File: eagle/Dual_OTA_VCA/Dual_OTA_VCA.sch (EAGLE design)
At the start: 31 parts, among them IC1 LM13600N, IC2 NJM4580, T1 2SA1015

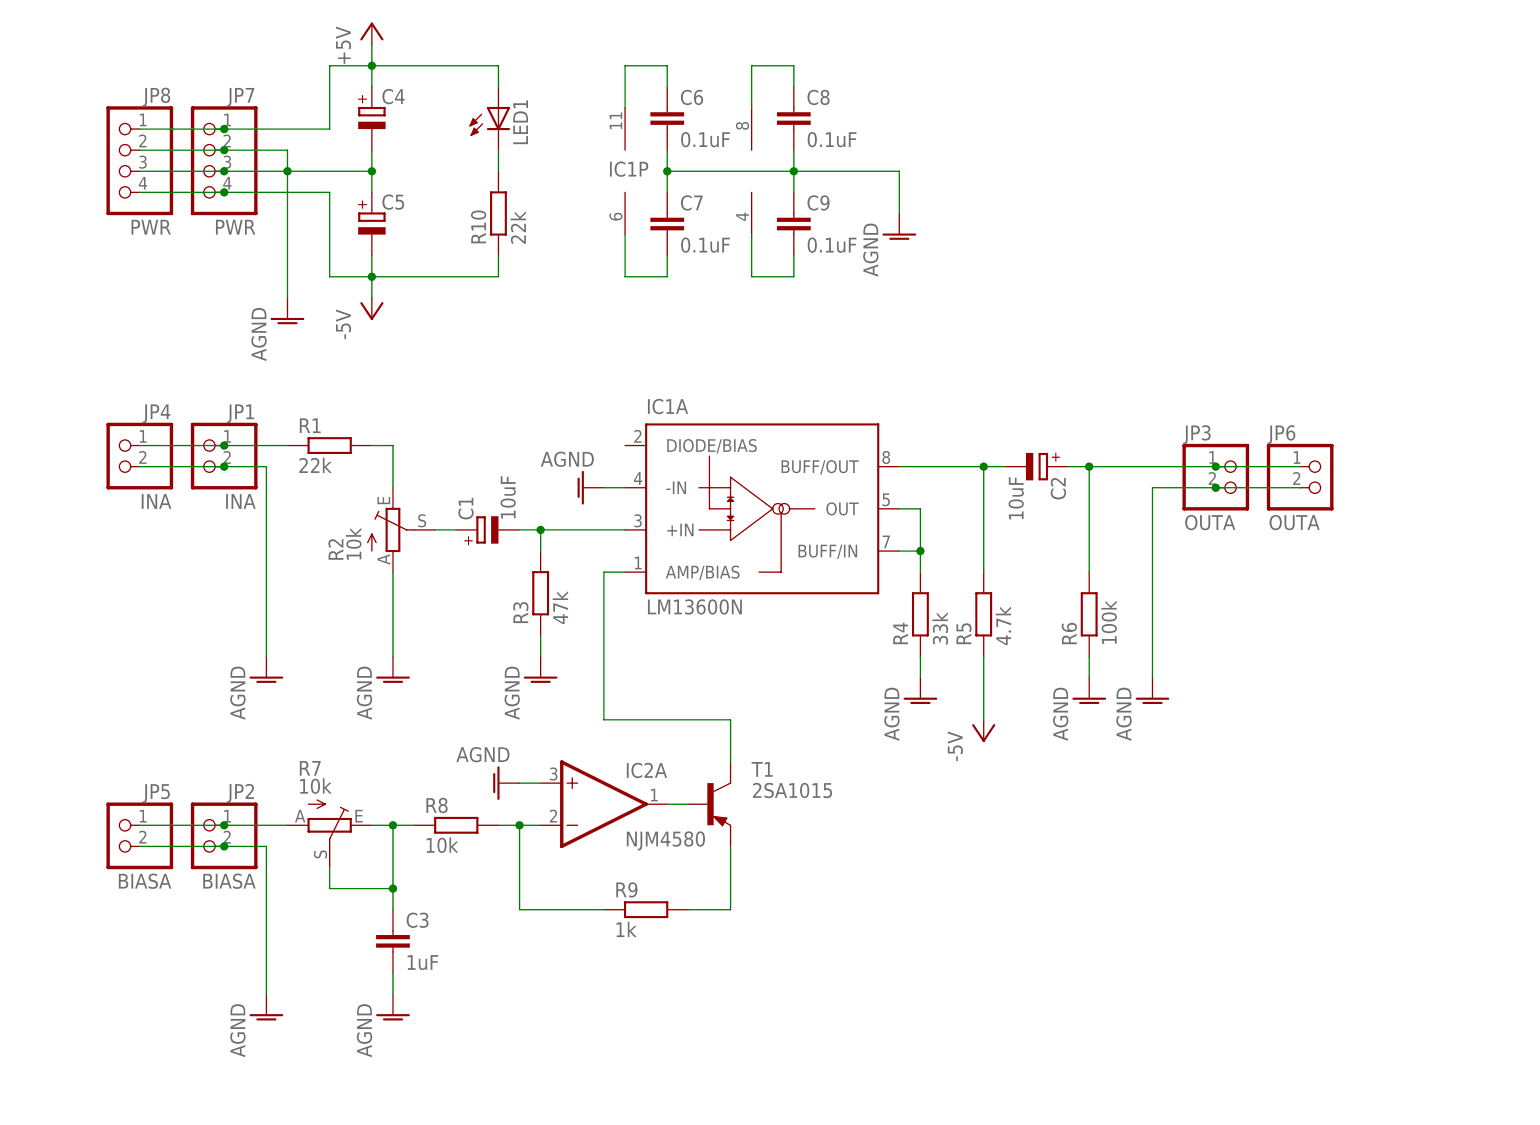
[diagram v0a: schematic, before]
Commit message: Add Bias IN Test
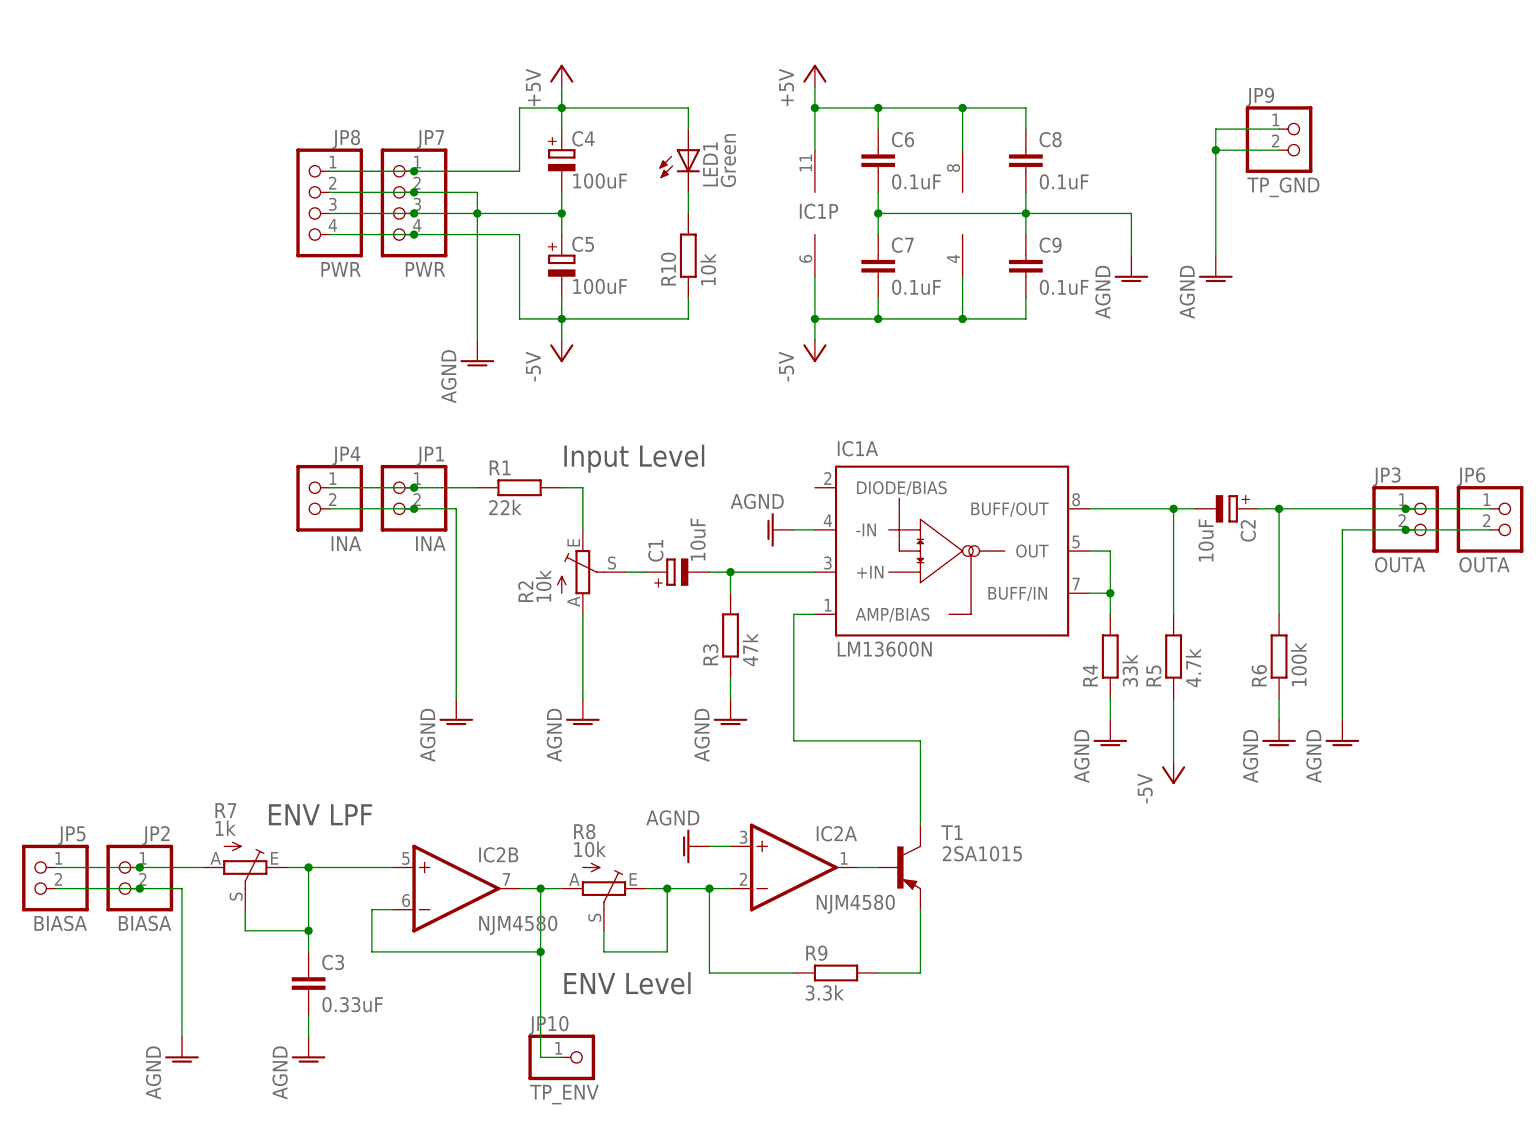
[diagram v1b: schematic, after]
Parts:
- added JP10: TP_ENV, pinhead:PINHD-1X1
- added JP9: TP_GND, pinhead:PINHD-1X2
- C3: value 1uF -> 0.33uF
- C4, C5: value (none) -> 100uF
- LED1: value (none) -> Green
- R10: value 22k -> 10k
- R7: value 10k -> 1k
- R8: device rcl:R-EU_0207/7 -> pot:TRIM_EU-B25P
- R9: value 1k -> 3.3k
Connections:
- removed net N$16: C6.1, IC1P.V+
- removed net N$18: C7.2, IC1P.V-
- removed net N$19: C8.1, IC2P.V+
- removed net N$20: C9.2, IC2P.V-
- new net N$13: IC2B.-IN, IC2B.OUT, JP10.1, R8.A
- net +5V: now also C6.1, C8.1, IC1P.V+, IC2P.V+
- net -5V: now also C7.2, C9.2, IC1P.V-, IC2P.V-
- net AGND: now also JP9.1, JP9.2
- net N$7: now also IC2B.+IN; no longer R8.1
- net N$9: now also R8.E, R8.S; no longer R8.2
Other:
- note added: "ENV LPF"
- note added: "ENV Level"
- note added: "Input Level"
- moved on the sheet: C1, C2, C3, C4, C5, C6, C7, C8, C9, IC1A, IC1P, IC2A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

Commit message: Update Schematics
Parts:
- added C10, C11: 0.1uF, rcl:C-EU025-024X044
- added IC3: LM4558N, linear:LM4558N
- added R11, R12: 10k, rcl:R-EU_0207/7
- R7: value 1k -> 10k
- R8: value 10k -> 100k
- R9: value 3.3k -> 1k
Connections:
- removed net N$13: IC2B.-IN, IC2B.OUT, JP10.1, R8.A
- new net N$16: R11.2, R7.E
- new net N$17: IC3A.+IN, R7.S
- new net N$18: IC3A.-IN, IC3A.OUT, R8.A, R8.S
- new net N$19: C3.1, IC2B.+IN, R8.E
- net +5V: now also C10.1, IC3P.V+
- net -5V: now also C11.2, IC3P.V-
- net AGND: now also C10.2, C11.1, R7.A
- net N$10: now also R11.1; no longer R7.A
- net N$7: now also IC2B.-IN, IC2B.OUT, JP10.1, R12.1; no longer C3.1, IC2B.+IN, R7.E, R7.S
- net N$9: now also R12.2; no longer R8.E, R8.S
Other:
- moved on the sheet: C1, C2, C3, C4, C5, C6, C7, C8, C9, IC1A, IC1P, IC2A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

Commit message: 1ch Test
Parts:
- removed R11: 10k, rcl:R-EU_0207/7
- R1: value 22k -> 82k
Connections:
- removed net N$16: R11.2, R7.E
- net N$10: now also R7.E; no longer R11.1
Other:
- moved on the sheet: JP2, JP5
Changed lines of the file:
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@@
 <part name="JP1" library="pinhead" deviceset="PINHD-1X2" device="" value="INA"/>
 <part name="AGND3" library="supply1" deviceset="AGND" device=""/>
-<part name="R1" library="rcl" deviceset="R-EU_" device="0207/7" value="22k"/>
+<part name="R1" library="rcl" deviceset="R-EU_" device="0207/7" value="82k"/>
 <part name="R2" library="pot" deviceset="TRIM_EU-" device="B25P" value="10k"/>
 <part name="AGND4" library="supply1" deviceset="AGND" device=""/>
@@
 <part name="AGND12" library="supply1" deviceset="AGND" device=""/>
 <part name="JP10" library="pinhead" deviceset="PINHD-1X1" device="" value="TP_ENV"/>
-<part name="R11" library="rcl" deviceset="R-EU_" device="0207/7" value="10k"/>
 <part name="AGND14" library="supply1" deviceset="AGND" device=""/>
 <part name="IC3" library="linear" deviceset="*4558" device="N" technology="LM"/>
@@
 <instance part="R7" gate="1" x="45.72" y="63.5"/>
 <instance part="C3" gate="G$1" x="86.36" y="55.88"/>
-<instance part="JP2" gate="G$1" x="22.86" y="68.58" rot="MR0"/>
-<instance part="AGND2" gate="VR1" x="30.48" y="45.72"/>
+<instance part="JP2" gate="G$1" x="27.94" y="68.58" rot="MR0"/>
+<instance part="AGND2" gate="VR1" x="35.56" y="45.72"/>
 <instance part="AGND9" gate="VR1" x="86.36" y="45.72"/>
 <instance part="IC2" gate="A" x="137.16" y="60.96"/>
@@
 </instance>
 <instance part="JP4" gate="G$1" x="78.74" y="104.14" rot="MR0"/>
-<instance part="JP5" gate="G$1" x="12.7" y="68.58" rot="MR0"/>
+<instance part="JP5" gate="G$1" x="17.78" y="68.58" rot="MR0"/>
 <instance part="JP6" gate="G$1" x="223.52" y="101.6"/>
 <instance part="IC2" gate="P" x="157.48" y="139.7"/>
@@
 <instance part="AGND12" gate="VR1" x="205.74" y="127"/>
 <instance part="JP10" gate="G$1" x="121.92" y="43.18"/>
-<instance part="R11" gate="G$1" x="38.1" y="71.12"/>
 <instance part="AGND14" gate="VR1" x="45.72" y="45.72"/>
 <instance part="IC3" gate="A" x="58.42" y="60.96"/>
@@
 <pinref part="JP2" gate="G$1" pin="2"/>
 <pinref part="AGND2" gate="VR1" pin="AGND"/>
-<wire x1="25.4" y1="68.58" x2="30.48" y2="68.58" width="0.1524" layer="91"/>
-<wire x1="30.48" y1="68.58" x2="30.48" y2="48.26" width="0.1524" layer="91"/>
+<wire x1="30.48" y1="68.58" x2="35.56" y2="68.58" width="0.1524" layer="91"/>
+<wire x1="35.56" y1="68.58" x2="35.56" y2="48.26" width="0.1524" layer="91"/>
 <pinref part="JP5" gate="G$1" pin="2"/>
-<wire x1="15.24" y1="68.58" x2="25.4" y2="68.58" width="0.1524" layer="91"/>
-<junction x="25.4" y="68.58"/>
+<wire x1="20.32" y1="68.58" x2="30.48" y2="68.58" width="0.1524" layer="91"/>
+<junction x="30.48" y="68.58"/>
 </segment>
 <segment>
@@
 <pinref part="JP2" gate="G$1" pin="1"/>
 <pinref part="JP5" gate="G$1" pin="1"/>
-<wire x1="15.24" y1="71.12" x2="25.4" y2="71.12" width="0.1524" layer="91"/>
-<pinref part="R11" gate="G$1" pin="1"/>
-<wire x1="25.4" y1="71.12" x2="33.02" y2="71.12" width="0.1524" layer="91"/>
-<junction x="25.4" y="71.12"/>
+<wire x1="20.32" y1="71.12" x2="30.48" y2="71.12" width="0.1524" layer="91"/>
+<junction x="30.48" y="71.12"/>
+<pinref part="R7" gate="1" pin="E"/>
+<wire x1="45.72" y1="68.58" x2="45.72" y2="71.12" width="0.1524" layer="91"/>
+<wire x1="30.48" y1="71.12" x2="45.72" y2="71.12" width="0.1524" layer="91"/>
 </segment>
 </net>
@@
 </segment>
 </net>
-<net name="N$16" class="0">
-<segment>
-<pinref part="R7" gate="1" pin="E"/>
-<wire x1="45.72" y1="68.58" x2="45.72" y2="71.12" width="0.1524" layer="91"/>
-<pinref part="R11" gate="G$1" pin="2"/>
-<wire x1="45.72" y1="71.12" x2="43.18" y2="71.12" width="0.1524" layer="91"/>
-</segment>
-</net>

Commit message: begin 2ch
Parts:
- added C12, C13: 0.1uF, rcl:C-EU025-024X044
- added C14, C15: 10uF, rcl:CPOL-EUE2.5-7
- added C16: 0.33uF, rcl:C-EU050-030X075
- added IC4: NJM4580, linear:LM4558N
- added JP11, JP14: INB, pinhead:PINHD-1X2
- added JP12, JP16: OUTB, pinhead:PINHD-1X2
- added JP13, JP15: BIASB, pinhead:PINHD-1X2
- added JP17: TP_ENVB, pinhead:PINHD-1X1
- added R11: 82k, rcl:R-EU_0207/7
- added R13, R18: 10k, pot:TRIM_EU-B25P
- added R14: 47k, rcl:R-EU_0207/7
- added R15: 33k, rcl:R-EU_0207/7
- added R16: 4.7k, rcl:R-EU_0207/7
- added R17: 100k, rcl:R-EU_0207/7
- added R19: 1k, rcl:R-EU_0207/7
- added R20: 100k, pot:TRIM_EU-B25P
- added R21: 10k, rcl:R-EU_0207/7
- added T2: 2SA1015, transistor-neu-to92:-PNP-TO92-ECB
- JP10: value TP_ENV -> TP_ENVA
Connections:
- new net N$13: IC3B.+IN, R18.S
- new net N$16: JP11.1, JP14.1, R11.1
- new net N$20: R11.2, R13.E
- new net N$21: C14.+, R13.S
- new net N$22: C14.-, IC1B.+IN, R14.2
- new net N$23: IC1B.BUFF/IN, IC1B.OUT, R15.2
- new net N$24: C15.-, IC1B.BUFF/OUT, R16.2
- new net N$25: C15.+, JP12.1, JP16.1, R17.2
- new net N$26: JP13.1, JP15.1, R18.E
- new net N$27: IC2B.-IN, R19.1, R21.2
- new net N$28: R19.2, T2.E
- new net N$29: IC2B.OUT, T2.B
- new net N$30: IC1B.AMP/BIAS, T2.C
- new net N$32: IC3B.-IN, IC3B.OUT, R20.A, R20.S
- new net N$33: C16.1, IC4B.+IN, R20.E
- new net N$34: IC4B.-IN, IC4B.OUT, JP17.1, R21.1
- net +5V: now also C12.1, IC4P.V+
- net -5V: now also C13.2, IC4P.V-, R16.1
- net AGND: now also C12.2, C13.1, C16.2, IC1B.-IN, IC2B.+IN, JP11.2, JP12.2, JP13.2, JP14.2, JP15.2, JP16.2, R13.A, R14.1, R15.1, R17.1, R18.A
- net N$19: now also IC4A.+IN; no longer IC2B.+IN
- net N$7: now also IC4A.-IN, IC4A.OUT; no longer IC2B.-IN, IC2B.OUT
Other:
- moved on the sheet: C1, C10, C11, C2, C3, C4, C5, C6, C7, C8, C9, IC1A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

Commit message: Update the eagle files
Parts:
- C6, C7: device rcl:C-EU025-024X044 -> rcl:C-EU050-024X044
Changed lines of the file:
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@@
 <part name="LED1" library="led" deviceset="LED" device="3MM" value="Green"/>
 <part name="R10" library="rcl" deviceset="R-EU_" device="0207/7" value="10k"/>
-<part name="C6" library="rcl" deviceset="C-EU" device="025-024X044" value="0.1uF"/>
-<part name="C7" library="rcl" deviceset="C-EU" device="025-024X044" value="0.1uF"/>
+<part name="C6" library="rcl" deviceset="C-EU" device="050-024X044" value="0.1uF"/>
+<part name="C7" library="rcl" deviceset="C-EU" device="050-024X044" value="0.1uF"/>
 <part name="C8" library="rcl" deviceset="C-EU" device="025-024X044" value="0.1uF"/>
 <part name="C9" library="rcl" deviceset="C-EU" device="025-024X044" value="0.1uF"/>

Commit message: Board Design
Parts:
- R1, R11: value 82k -> 56k
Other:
- moved on the sheet: C1, C10, C11, C12, C13, C14, C15, C16, C2, C3, C4, C5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
